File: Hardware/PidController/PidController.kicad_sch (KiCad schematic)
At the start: 49 parts, among them J1 Conn_01x03, J2 Conn_01x03, J3 Conn_01x04, J4 Conn_01x06, J5 Motor_x02, J6 Conn_01x04, Q1 BC817, Q2 BTA16-600B, T1 GG_Transformer_1P_1S, U1 LM317_TO-220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

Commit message: First tests done, first PID params tuning
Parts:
- removed C2: 220mF, Capacitor_THT:CP_Radial_D8.0mm_P5.00mm, symbol Device:C_Polarized
- removed D2, D3, D4: D, PCB_Library:D_SMD_L, symbol Device:D
- removed L1: L, PCB_Library:L_2R2_SMD, symbol Device:L
- removed Q1: BC817, Package_TO_SOT_SMD:SOT-23, symbol Transistor_BJT:BC817
- removed Q2: BTA16-600B, Package_TO_SOT_THT:TO-220-3_Vertical, symbol Triac_Thyristor:BTA16-600B
- removed T1: GG_Transformer_1P_1S, PCB_Library:Transformer_2VA_1xSec, symbol GG_Library:GG_Transformer_1P_1S
- removed U3: MOC3023M, PCB_Library:MOC3023_W7.62mm, symbol Relay_SolidState:MOC3023M
- added #D1, #D2: D, PCB_Library:D_SMD_L, symbol Device:D
- added #R3: 1K, Resistor_SMD:R_1206_3216Metric_Pad1.30x1.75mm_HandSolder, symbol Device:R
- added C10, C8: 100mf, PCB_Library:CP_Radial_D18.0mm_P7.50mm, symbol Device:C_Polarized
- added C11: 4.7uF, PCB_Library:C_Film_5.08, symbol Device:C
- added C12: 1000mF, PCB_Library:CP_Radial_D8.0mm_P5.00mm, symbol Device:C_Polarized
- added C13, C9: 100nF, Capacitor_SMD:C_0805_2012Metric_Pad1.18x1.45mm_HandSolder, symbol Device:C
- added C2: 100nF, LED_SMD:LED_1210_3225Metric, symbol Device:C
- added C?: 1nF, Capacitor_SMD:C_0805_2012Metric_Pad1.18x1.45mm_HandSolder, symbol Device:C
- added D10: RHRP15120, PCB_Library:D_TO-220-2_Vertical, symbol Device:D
- added D2: LED, LED_SMD:LED_2010_5025Metric, symbol Device:LED
- added D7: Bat54, PCB_Library:D_SOT-23_ANK, symbol Device:D
- added D8: D_Bridge_-AA+, PCB_Library:Diode_Bridge_300V, symbol Device:D_Bridge_-AA+
- added D9: LED, LED_SMD:LED_1210_3225Metric_Pad1.42x2.65mm_HandSolder, symbol Device:LED
- added F1: Fuse, PCB_Library:Fuse_5X20, symbol Device:Fuse
- added Q1: BC640, PCB_Library:TO-92_delta, symbol Device:Q_NPN_ECB
- added Q2: BC639, PCB_Library:TO-92_delta, symbol Transistor_BJT:BC636
- added Q3: Q_NMOS_GDS, Package_TO_SOT_THT:TO-247-3_Vertical, symbol Device:Q_NMOS_GDS
- added T2: Transformer_1P_1S, PCB_Library:Transformer_Toroid_Horizontal_D18.0mm, symbol Device:Transformer_1P_1S
- added U3: 4071, Package_DIP:DIP-14_W8.89mm_SMDSocket_LongPads, symbol 4xxx:4071
- #R1: value 330 -> 470
- #R2: value 330 -> 4.7K
- C3: footprint Capacitor_THT:CP_Radial_D8.0mm_P5.00mm -> PCB_Library:CP_Radial_D8.0mm_P5.00mm
- C7: value 0 -> 47nF
- D1: footprint PCB_Library:D_SMD_L -> Diode_THT:D_5KPW_P12.70mm_Horizontal
- D5: value D -> Bat54; footprint PCB_Library:D_SMD_L -> PCB_Library:D_SOT-23_ANK
- J2: footprint PCB_Library:GG_PinHeader_1x03 -> PCB_Library:JWT_1x03_P3.96mm_Vertical
- R1: value 220 -> 1K
- R11: value 220 -> 10
- R12: value 10 -> 47K
- R13: value 100 -> 47K
- R14: value 220 -> 100; footprint Resistor_SMD:R_1206_3216Metric_Pad1.30x1.75mm_HandSolder -> Resistor_THT:R_Axial_DIN0309_L9.0mm_D3.2mm_P12.70mm_Horizontal
- R15: value 100 -> 220
- R3: value 47k -> 1K
- R4, R8: value 4.7k -> 1K
- R5: value 1.5k -> 2.2K
- R7: value 330 -> 220
- R9: value 4.7k -> 10
- U1: footprint Package_TO_SOT_THT:TO-220-3_Vertical -> PCB_Library:TO-263-2
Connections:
- net AC10V_2 is gone; now on net +14V: D1.2 (A)
- net AC220V_L: now also F1.1; no longer J5.1 (Pin_1), R12.1
- net AC220V_N: now also D8.3; no longer C7.2, R14.2
- net GND: now also R8.1, C12.2, C13.2, C2.2, C?.2, Q2.2 (C), T2.1 (AA), U3.7 (VSS); no longer R4.2, R9.2
- net RST: now also U2.6 (C1)
- net +11V: now reaches R15.2
- net +11V: now also U2.12 (VIN), C13.1, D2.1 (K)
- net at R14.1: now also Q3.1 (G), T2.3 (SA)
- net Orange: now reaches #R1.1, #R2.1
- net GNDPWR: now reaches R13.1
- net GNDPWR: now also R14.2, C10.2, C8.2, D8.1 (-), Q3.3 (S), T2.4 (SB)
- net at D5.1 (K): now also R3.1, R4.2; no longer U1.3 (VI)
- net at R4.1: now also R8.2, D7.2 (A); no longer R3.2
- net Blue/White: now reaches #U1.2 (K), #U1.4 (E)
- net Green: now reaches #R2.2, #U1.3 (C)
- net at R1.1, U2.18 (D3): now also C?.1
- net at R11.1: now also R9.1, C11.1
- net at R11.2: now also R9.2, Q1.1 (E), Q2.1 (E); no longer U2.1 (B2)
- net at J5.2 (Pin_2): now also D10.2 (A), Q3.2 (D)
- net at R12.2: now also J5.1 (Pin_1), C10.1, C8.1, D10.1 (K), D8.4 (+)
- net +7.5V renamed +14V
- net +14V: now also R3.2, C9.2, Q1.2 (C), U3.14 (VDD); no longer R8.1, U2.12 (VIN)
- removed net ZERO_CROSS: R8.2, R9.1, U2.23 (B0)
- new net: Q1.3 (B), Q2.3 (B), U3.10, U3.11, U3.3, U3.4
- new net: D1.1 (K), D2.2 (A), R15.1
- new net: D9.2 (A), R12.1
- new net: C11.2, T2.2 (AB)
- new net: #D1.2 (A), #D2.1 (K), #R3.2
- new net: C7.2, D5.2 (A), D7.1 (K), U3.1, U3.12, U3.13, U3.2, U3.5, U3.6, U3.8, U3.9
- new net: D9.1 (K), R13.2
- new net +22V: C12.1, C2.1, U1.3 (VI)
- new net 220V_L: D8.2, F1.2
- new net PWM: C7.1, U2.1 (B2)
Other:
- note added: "Tacho"
- moved on the sheet: C1, C3, C4, C5, C6, D6, J1, J2, J3, J4, J6, R1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

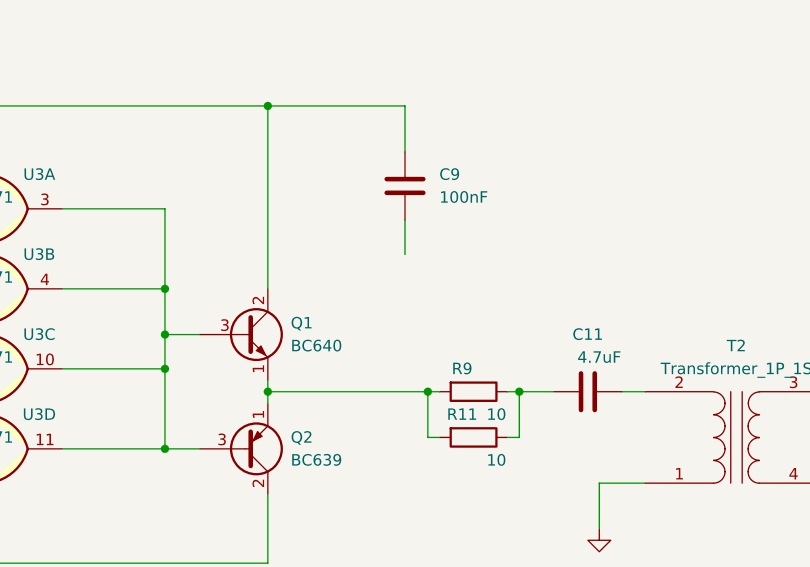
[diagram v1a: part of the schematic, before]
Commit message: Improve PID parameters with bench drill
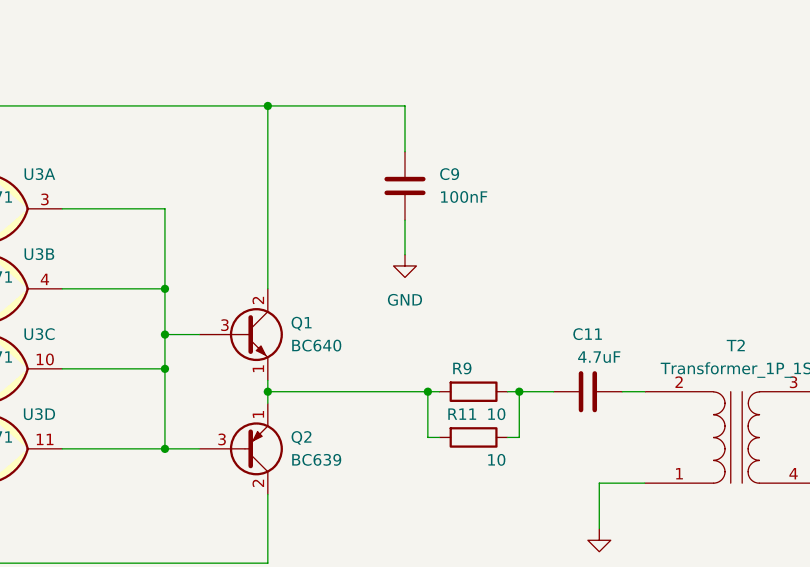
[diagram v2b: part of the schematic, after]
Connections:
- net GND: now also C9.1
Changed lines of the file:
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@@
+    (pin "1")
+  )
+  (symbol (lib_id "power:GND") (at 307.34 166.37 0) (unit 1)
+    (in_bom yes) (on_board yes) (fields_autoplaced)
+    (property "Reference" "#PWR?" (id 0) (at 307.34 172.72 0)
+      (effects (font (size 1.27 1.27)) hide)
+    )
+    (property "Value" "GND" (id 1) (at 307.34 171.45 0))
+    (property "Footprint" "" (id 2) (at 307.34 166.37 0)
+      (effects (font (size 1.27 1.27)) hide)
+    )
+    (property "Datasheet" "" (id 3) (at 307.34 166.37 0)
+      (effects (font (size 1.27 1.27)) hide)
+    )
     (pin "1")
   )
@@
       (reference "#PWR0102") (unit 1) (value "GND") (footprint "")
     )
+    (path "/5f734aaa-2969-44ca-8f3a-d5537c454e57"
+      (reference "#PWR?") (unit 1) (value "GND") (footprint "")
+    )
     (path "/f5246526-8b21-4e4d-b389-b9b22d7521f7"
